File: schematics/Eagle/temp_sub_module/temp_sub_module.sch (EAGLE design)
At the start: 4 parts

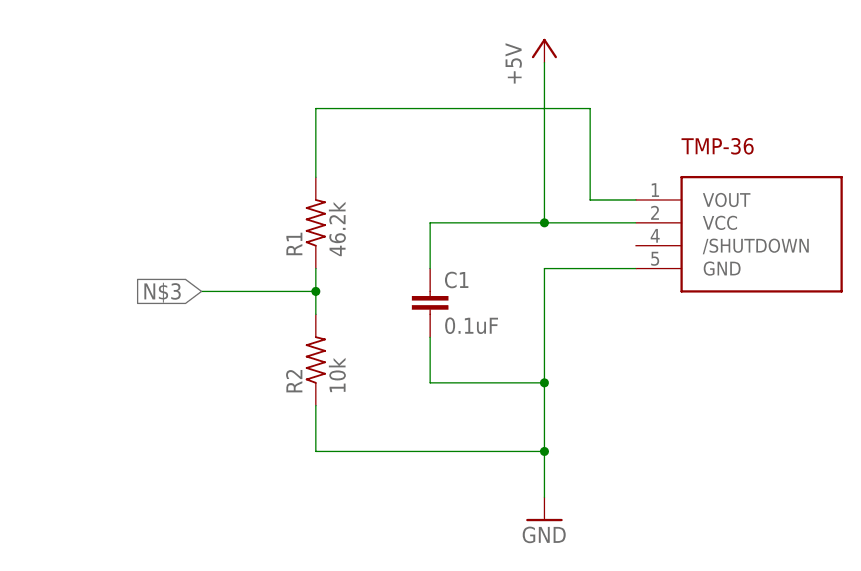
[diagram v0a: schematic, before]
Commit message: added the rest of the schematics
created schematics for the remaining sub-modules. Also fixed up some pin assignments for other schematics.

Added voltage divider to 5V analog sensors for 3.3V operation with PIC
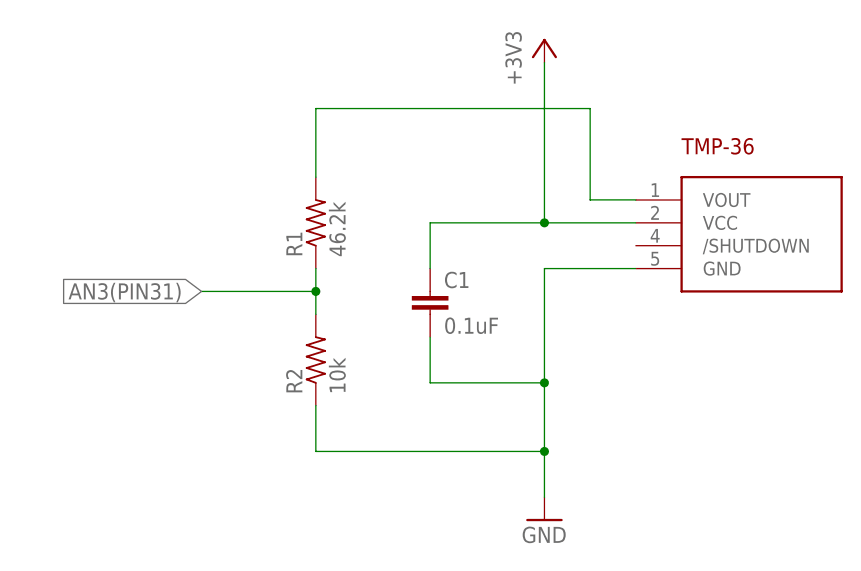
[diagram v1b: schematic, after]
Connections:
- net +5V renamed +3V3
- net N$3 renamed AN3(PIN31)
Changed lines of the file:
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@@
 <setting verticaltext="up"/>
 </settings>
-<grid distance="0.1" unitdist="inch" unit="inch" style="lines" multiple="1" display="yes" altdistance="0.01" altunitdist="inch" altunit="inch"/>
+<grid distance="0.1" unitdist="inch" unit="inch" style="lines" multiple="1" display="no" altdistance="0.01" altunitdist="inch" altunit="inch"/>
 <layers>
 <layer number="1" name="Top" color="4" fill="1" visible="no" active="no"/>
@@
 <parts>
 <part name="U$1" library="TMP36" deviceset="TMP36" device=""/>
-<part name="P+1" library="supply1" deviceset="+5V" device=""/>
 <part name="GND1" library="supply1" deviceset="GND" device=""/>
 <part name="R1" library="resistor" deviceset="R-US_" device="0204/2V" value="46.2k"/>
 <part name="R2" library="resistor" deviceset="R-US_" device="0204/2V" value="10k"/>
 <part name="C1" library="rcl" deviceset="C-EU" device="025-024X044" value="0.1uF"/>
+<part name="+3V1" library="supply1" deviceset="+3V3" device=""/>
 </parts>
 <sheets>
@@
 <instances>
 <instance part="U$1" gate="G$1" x="55.88" y="68.58"/>
-<instance part="P+1" gate="1" x="40.64" y="96.52"/>
 <instance part="GND1" gate="1" x="40.64" y="43.18"/>
 <instance part="R1" gate="G$1" x="15.24" y="76.2" rot="R90"/>
 <instance part="R2" gate="G$1" x="15.24" y="60.96" rot="R90"/>
 <instance part="C1" gate="G$1" x="27.94" y="68.58"/>
+<instance part="+3V1" gate="G$1" x="40.64" y="96.52"/>
 </instances>
 <busses>
 </busses>
 <nets>
-<net name="+5V" class="0">
-<segment>
-<pinref part="U$1" gate="G$1" pin="VCC"/>
-<pinref part="P+1" gate="1" pin="+5V"/>
-<wire x1="50.8" y1="76.2" x2="40.64" y2="76.2" width="0.1524" layer="91"/>
-<wire x1="40.64" y1="76.2" x2="40.64" y2="93.98" width="0.1524" layer="91"/>
-<pinref part="C1" gate="G$1" pin="1"/>
-<wire x1="40.64" y1="76.2" x2="27.94" y2="76.2" width="0.1524" layer="91"/>
-<wire x1="27.94" y1="76.2" x2="27.94" y2="71.12" width="0.1524" layer="91"/>
-<junction x="40.64" y="76.2"/>
-</segment>
-</net>
 <net name="GND" class="0">
 <segment>
@@
 </segment>
 </net>
-<net name="N$3" class="0">
+<net name="AN3(PIN31)" class="0">
 <segment>
 <pinref part="R1" gate="G$1" pin="1"/>
@@
 </segment>
 </net>
+<net name="+3V3" class="0">
+<segment>
+<pinref part="U$1" gate="G$1" pin="VCC"/>
+<wire x1="50.8" y1="76.2" x2="40.64" y2="76.2" width="0.1524" layer="91"/>
+<wire x1="40.64" y1="76.2" x2="40.64" y2="93.98" width="0.1524" layer="91"/>
+<pinref part="C1" gate="G$1" pin="1"/>
+<wire x1="40.64" y1="76.2" x2="27.94" y2="76.2" width="0.1524" layer="91"/>
+<wire x1="27.94" y1="76.2" x2="27.94" y2="71.12" width="0.1524" layer="91"/>
+<junction x="40.64" y="76.2"/>
+<pinref part="+3V1" gate="G$1" pin="+3V3"/>
+</segment>
+</net>
